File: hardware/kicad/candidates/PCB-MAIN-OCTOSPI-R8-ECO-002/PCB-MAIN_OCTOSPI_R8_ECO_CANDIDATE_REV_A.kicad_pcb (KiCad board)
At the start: 6 copper layers, 110 x 75 mm, 251 parts, among them J10 U.FL-R-SMT-1(60), J11 USB4105-GF-A-120, J12 MEM2052-00-195-00-A, J13 504050-0291, J6 2336582-1, J7 2336582-1, J8 U.FL-R-SMT-1(60), J9 U.FL-R-SMT-1(60), Q1 MMBT3904,215, Q2 MMBT3904,215, Q3 MMBT3904,215, Q4 Si1016X-T1-GE3, U1 STM32U585VIT6Q, U10 E22-900M22S, U11 MDBT50Q-P1MV2, U13 TS3A27518EPWR, U14 ESDALC6V1-5P6, U15 ESDALC6V1-5P6, U16 SN74AXC8T245PWR, U17 SN74LVC32APWR, U18 SN74AXC1T45DRLR, U19 TPD4E05U06DQAR, U2 W25Q512JVFIQ, U20 TPD4E05U06DQAR, U21 TPD4E05U06DQAR, U22 TPD4E05U06DQAR, U23 TPD4E05U06DQAR, U24 TPD4E05U06DQAR, U25 TPD2EUSB30DRTR, U26 TPD2EUSB30DRTR, U27 TPD4E05U06DQAR, U3 LIS2DW12TR, U4 STTS22HTR, U5 LT6000IDCB#TRMPBF, U6 SN74LVC1G07DBVR, U7 SN74AXC8T245PWR, U8 BG95-M3, U9 MAX-M10S-00B, X1 SiT1552AI-JE-DCC-32.768D

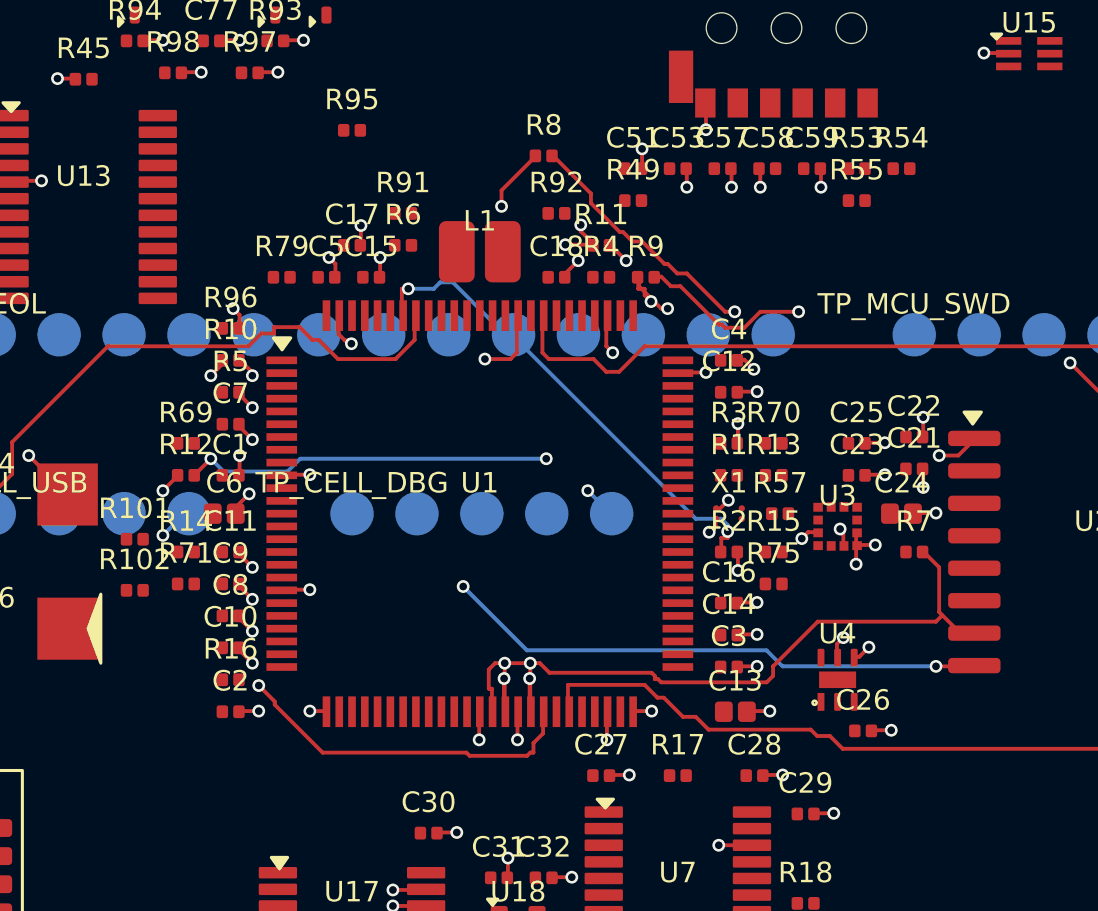
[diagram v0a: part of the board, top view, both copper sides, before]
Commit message: hardware: prioritize PCB-MAIN OctoSPI pad escapes
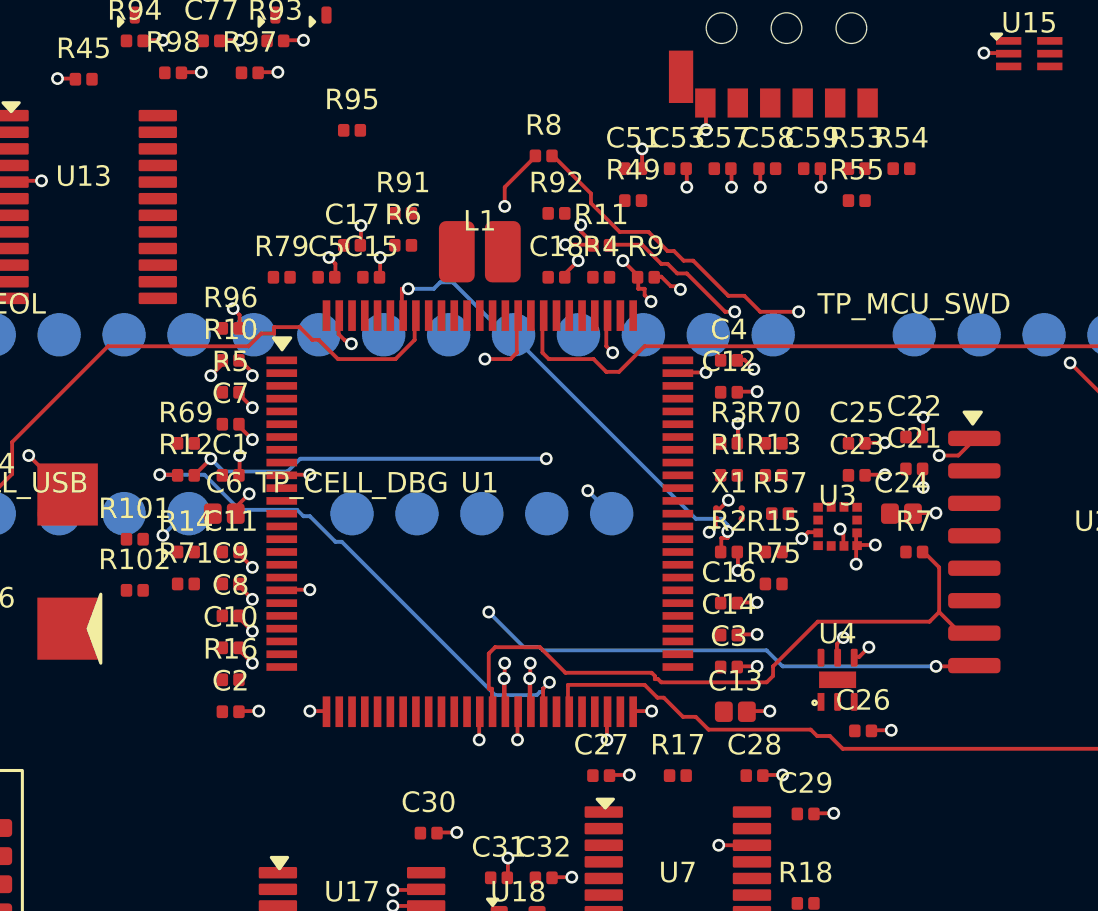
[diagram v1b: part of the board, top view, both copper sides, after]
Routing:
- net NOR_IO3_U1: track 24.1 -> 21.1 mm
- net NOR_NCS_U2: track 25.7 -> 26.5 mm
- net NOR_IO2_U2: track 31.1 -> 30.5 mm
- net NOR_IO0_U1: track 41.1 -> 40.5 mm
- net NOR_IO0_U2: track 25.4 -> 24.9 mm
